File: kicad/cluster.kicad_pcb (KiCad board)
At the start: 2 copper layers, 24.5 x 33.5 mm, 16 parts, among them J1 Conn_01x07

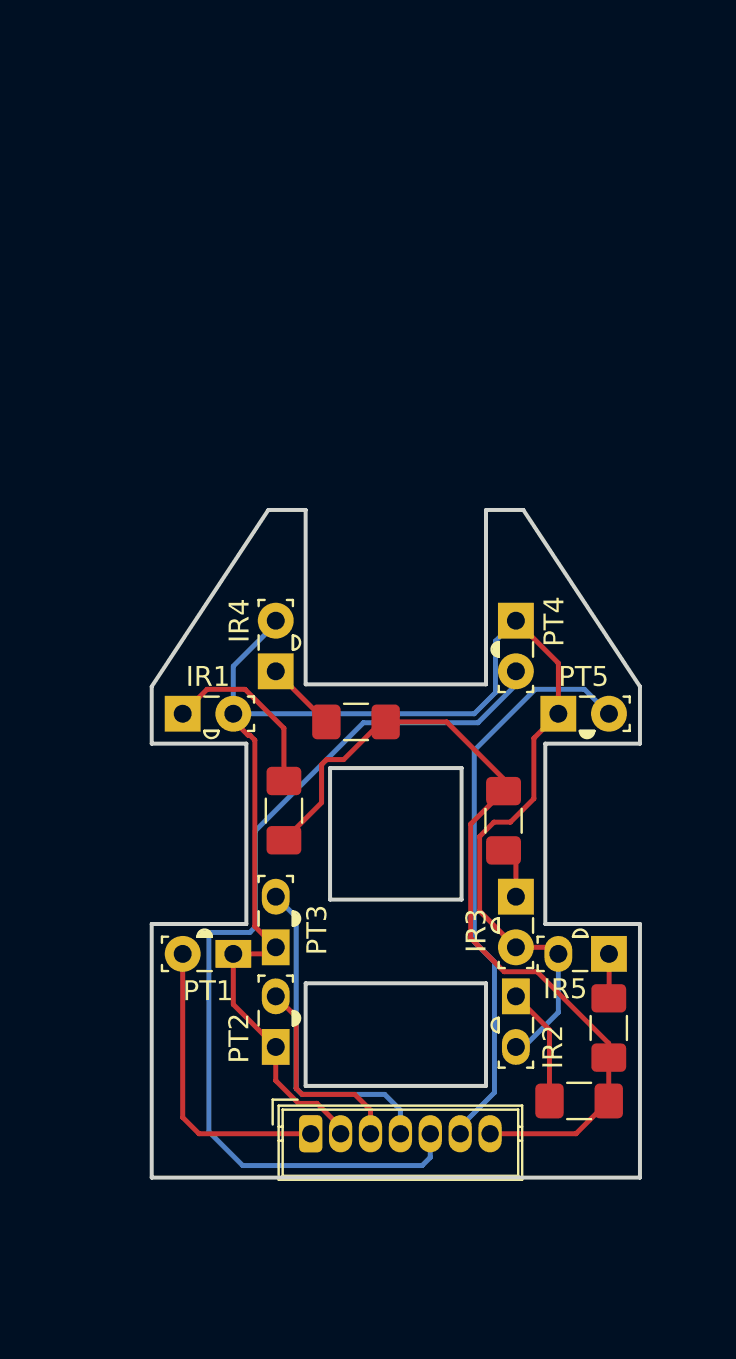
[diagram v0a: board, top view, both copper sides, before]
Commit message: Update the kicad design for the finger cluster
This brings the PCB design up to par with the current cluster design.
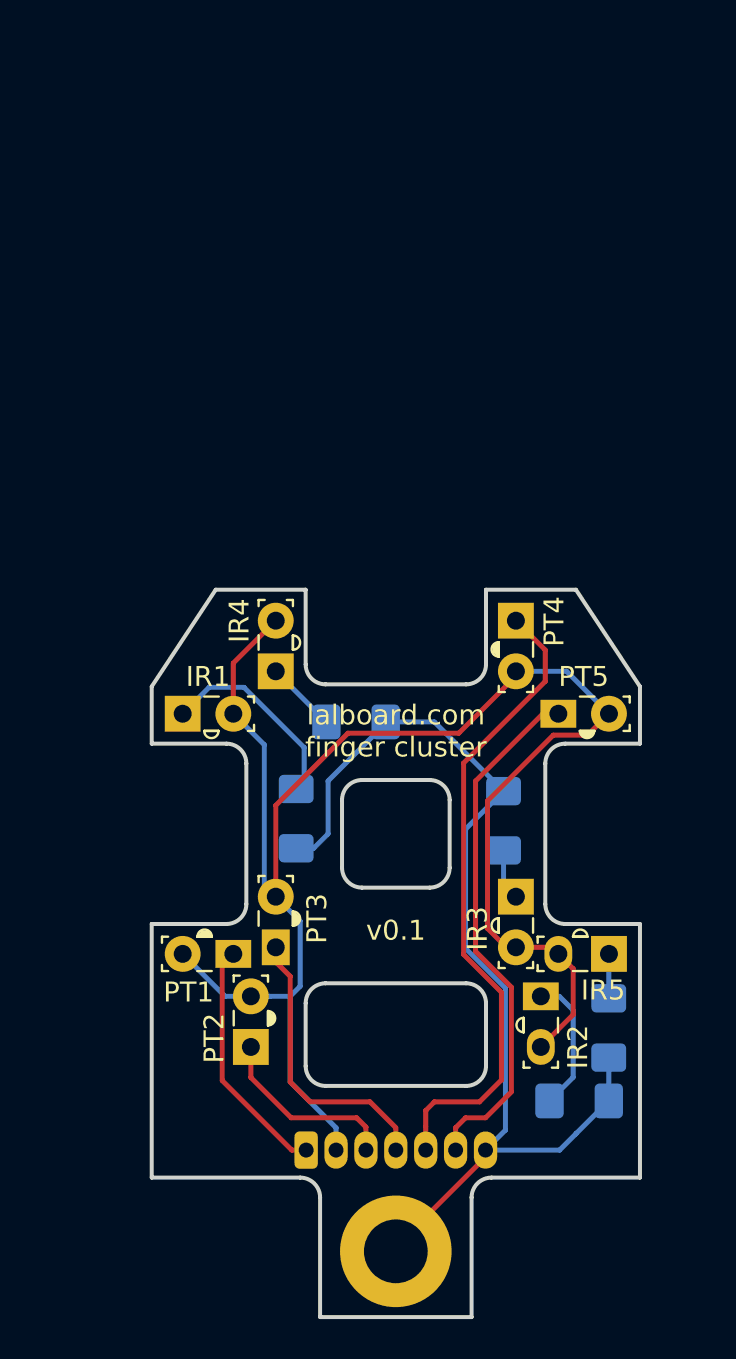
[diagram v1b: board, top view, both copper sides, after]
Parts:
- added REF**: MountingHole_3.2mm_M3, MountingHole:MountingHole_3.2mm_M3_DIN965_Pad, F.Cu at (165.3, 122.0)
- J1: footprint lalboard:JST_ZH_B7B-ZR_1x07_P1.50mm_Vertical -> lalboard:JST_ZH_S7B-ZR_1x07_P1.50mm_Horizontal; moved to B.Cu
- R1, R2, R3, R4, R5: moved to B.Cu
- moved IR2 1.25 mm to (172.6, 109.2)
- moved PT2 1.25 mm to (158.0, 111.8)
- moved J1 0.83 mm to (160.8, 116.9)
- moved R1 0.73 mm to (160.3, 100.3)
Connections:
- PT1 pad 1: +5V -> C1
- PT1 pad 2: C1 -> +5V
- PT2 pad 1: +5V -> C3
- PT2 pad 2: C3 -> +5V
- PT3 pad 1: +5V -> C4
- PT3 pad 2: C4 -> +5V
- PT4 pad 1: +5V -> C5
- PT4 pad 2: C5 -> +5V
- PT5 pad 1: +5V -> C6
- PT5 pad 2: C6 -> +5V
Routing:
- net C5: track 47.2 -> 32.6 mm
- net GND: track 43.5 -> 52.5 mm
- net +5V: track 78.1 -> 86.4 mm
- net C1: track 14.8 -> 12.2 mm
- net C4: track 16.9 -> 14.4 mm
- net C6: track 28.9 -> 26.6 mm
- net Net-(IR2-Pad1): track 5.95 -> 6.96 mm
- net Net-(IR1-Pad1): track 9.04 -> 9.97 mm
- net C3: track 10.4 -> 9.49 mm
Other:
- board size 24.5 x 33.5 mm -> 24.5 x 36.5 mm
- board text added: "Min internal corner radius: .8mm (for all internal corners)"
- board text added: "lalboard.com finger cluster"
- board text added: "v0.1"

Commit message: Update kicad design for finger cluster
This adds ground/+5v planes, some thicker traces, and moves the +5v pin
to pin 1 of the connector.

Thanks to @rutgervana for taking a look at the design and making
suggestions/showing example improvements.
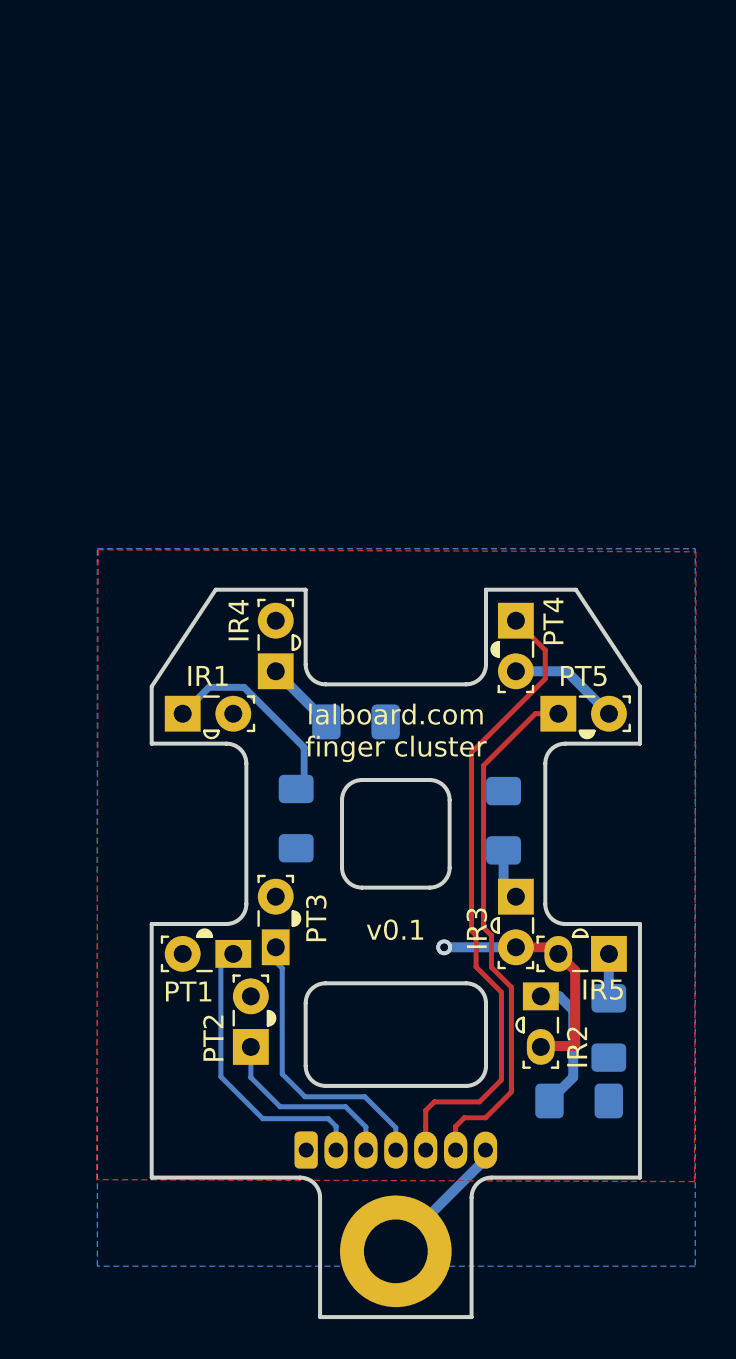
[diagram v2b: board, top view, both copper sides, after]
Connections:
- J1 pad 1: C1 -> +5V
- J1 pad 2: +5V -> C1
- J1 pad 3: C3 -> C2
- J1 pad 4: C4 -> C3
- J1 pad 5: C5 -> C4
- J1 pad 6: C6 -> C5
- PT2 pad 1: C3 -> C2
- PT3 pad 1: C4 -> C3
- PT4 pad 1: C5 -> C4
- PT5 pad 1: C6 -> C5
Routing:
- net +5V: track 86.4 -> 18.4 mm, vias 0 -> 1
- net GND: track 52.5 -> 7.04 mm
- net C6: track 26.6 -> 0.00 mm
- net C4: track 14.4 -> 32.2 mm
- net C2: track 0.00 -> 9.49 mm
- net C5: track 32.6 -> 26.5 mm
- net C3: track 9.49 -> 14.4 mm
- net C1: track 12.2 -> 15.2 mm
- added copper zone on F.Cu, net +5V
- added copper zone on B.Cu, net GND
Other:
- net class Power added: clearance 0.2, trace_width 0.5, via_dia 0.8, via_drill 0.4

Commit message: Add a virtual "locating pin" to the cluster pcb sketch
This gives a reference point for the origin of the sketch, so the import
location can be set correctly when importing the outline into kicad.

Basically, you set the grid origin in kicad to the center of the circle
(assuming the locating pin is already in kicad) and then make a note of
the coordinates of that point. And then, when importing the outline, you
can specify those coordinates as the location, to ensure the origin of the
imported outline matches that of the existing/previous outline.
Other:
- board text added: "Coords for import: (152.85, 125.535)"

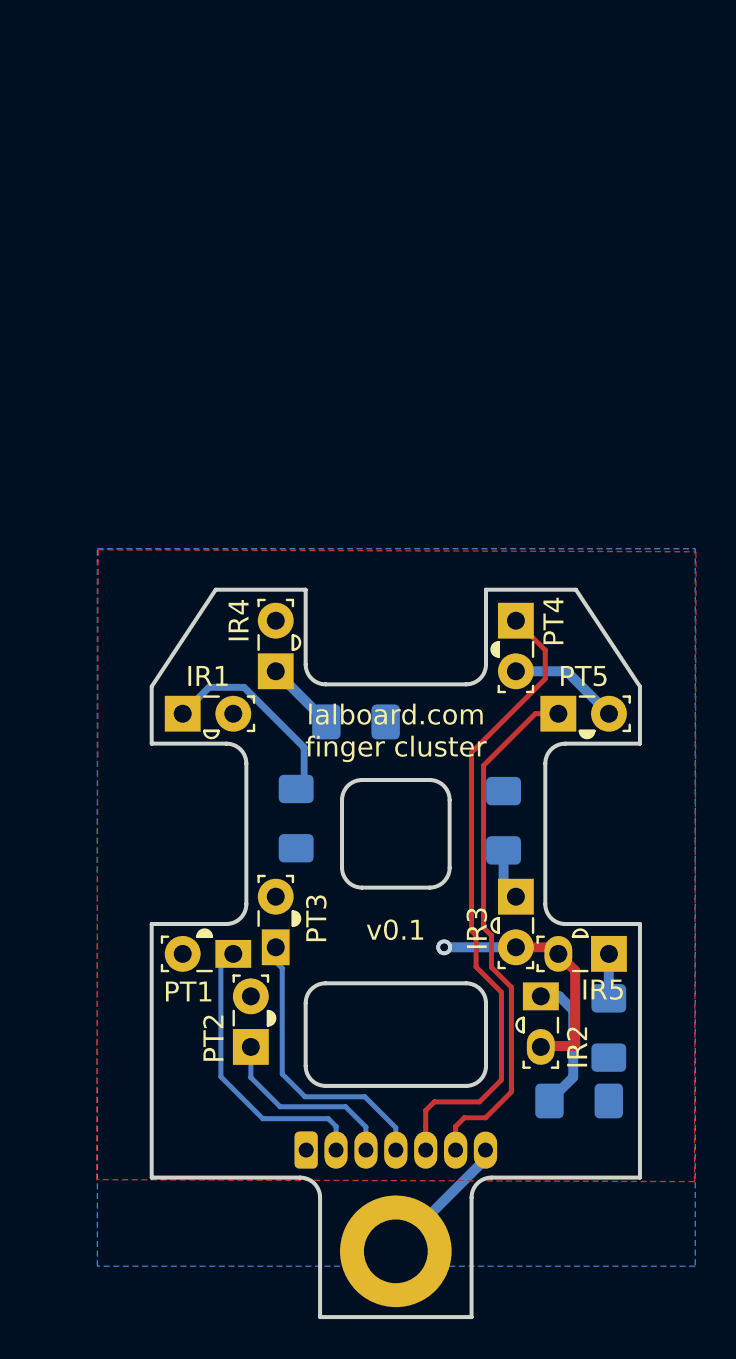
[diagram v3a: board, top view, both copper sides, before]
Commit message: Minor tweaks to the cluster pcb
- Move the identifying text to the bottom layer
- Disable some unused layers
- Move the design so that the import position is at an even (150, 100)
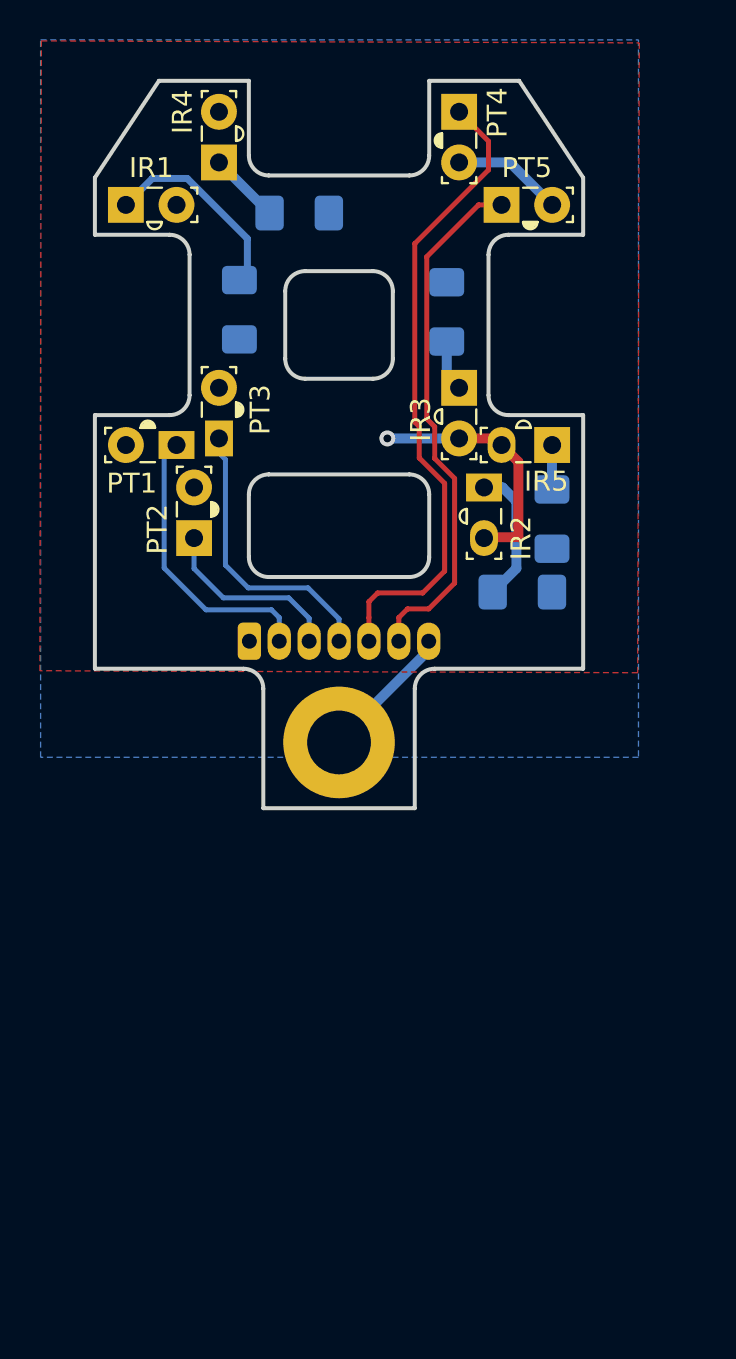
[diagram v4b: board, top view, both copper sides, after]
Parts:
- moved IR4 25.7 mm to (156.4, 67.4)
- moved R1 25.7 mm to (157.4, 74.8)
- moved R3 25.7 mm to (167.9, 74.9)
- moved IR1 25.7 mm to (151.8, 69.5)
- moved IR2 25.7 mm to (169.7, 83.7)
- moved IR3 25.7 mm to (168.5, 78.7)
- moved IR5 25.7 mm to (173.1, 81.6)
- moved J1 25.7 mm to (157.9, 91.4)
- moved PT1 25.7 mm to (154.3, 81.6)
- moved PT2 25.7 mm to (155.2, 86.2)
- moved PT3 25.7 mm to (156.4, 81.2)
- moved PT4 25.7 mm to (168.5, 64.9)
- moved PT5 25.7 mm to (170.6, 69.5)
- moved R2 25.7 mm to (171.6, 89.0)
- moved R4 25.7 mm to (160.5, 69.9)
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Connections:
- IR1 pad 1: Net-(IR1-Pad1) -> (no net)
- IR1 pad 2: +5V -> (no net)
- IR2 pad 1: Net-(IR2-Pad1) -> (no net)
- IR2 pad 2: +5V -> (no net)
- IR3 pad 1: Net-(IR3-Pad1) -> (no net)
- IR3 pad 2: +5V -> (no net)
- IR4 pad 1: Net-(IR4-Pad1) -> (no net)
- IR4 pad 2: +5V -> (no net)
- IR5 pad 1: Net-(IR5-Pad1) -> (no net)
- IR5 pad 2: +5V -> (no net)
- J1 pad 1: +5V -> (no net)
- J1 pad 2: C1 -> (no net)
- J1 pad 3: C2 -> (no net)
- J1 pad 4: C3 -> (no net)
- J1 pad 5: C4 -> (no net)
- J1 pad 6: C5 -> (no net)
- J1 pad 7: GND -> (no net)
- PT1 pad 1: C1 -> (no net)
- PT1 pad 2: +5V -> (no net)
- PT2 pad 1: C2 -> (no net)
- PT2 pad 2: +5V -> (no net)
- PT3 pad 1: C3 -> (no net)
- PT3 pad 2: +5V -> (no net)
- PT4 pad 1: C4 -> (no net)
- PT4 pad 2: +5V -> (no net)
- PT5 pad 1: C5 -> (no net)
- PT5 pad 2: +5V -> (no net)
- R1 pad 1: GND -> (no net)
- R1 pad 2: Net-(IR1-Pad1) -> (no net)
- R2 pad 1: GND -> (no net)
- R2 pad 2: Net-(IR2-Pad1) -> (no net)
- R3 pad 1: GND -> (no net)
- R3 pad 2: Net-(IR3-Pad1) -> (no net)
- R4 pad 1: GND -> (no net)
- R4 pad 2: Net-(IR4-Pad1) -> (no net)
- R5 pad 1: GND -> (no net)
- R5 pad 2: Net-(IR5-Pad1) -> (no net)
- REF** pad 1: GND -> (no net)
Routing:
- net (no net): track 0.00 -> 148.7 mm, vias 0 -> 1
- net C4: track 32.2 -> 0.00 mm
- net C5: track 26.5 -> 0.00 mm
- net +5V: track 18.4 -> 0.00 mm, vias 1 -> 0
- net C1: track 15.2 -> 0.00 mm
- net C3: track 14.4 -> 0.00 mm
- net Net-(IR1-Pad1): track 9.97 -> 0.00 mm
- net C2: track 9.49 -> 0.00 mm
- net GND: track 7.04 -> 0.00 mm
- net Net-(IR2-Pad1): track 6.96 -> 0.00 mm
- net Net-(IR4-Pad1): track 3.59 -> 0.00 mm
- net Net-(IR3-Pad1): track 2.58 -> 0.00 mm
- net Net-(IR5-Pad1): track 2.23 -> 0.00 mm
- added copper zone on B.Cu, net (none)
- added copper zone on F.Cu, net (none)
- removed copper zone on F.Cu, net +5V
- removed copper zone on B.Cu, net GND
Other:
- outline, holes or cut-outs redrawn
- board text added: "Coords for import: (150, 100)"
- board text added: "finger cluster v0.1"
- board text added: "lalboard.com"
- board text removed: "Coords for import: (152.85, 125.535)"
- board text removed: "lalboard.com finger cluster"
- board text removed: "v0.1"

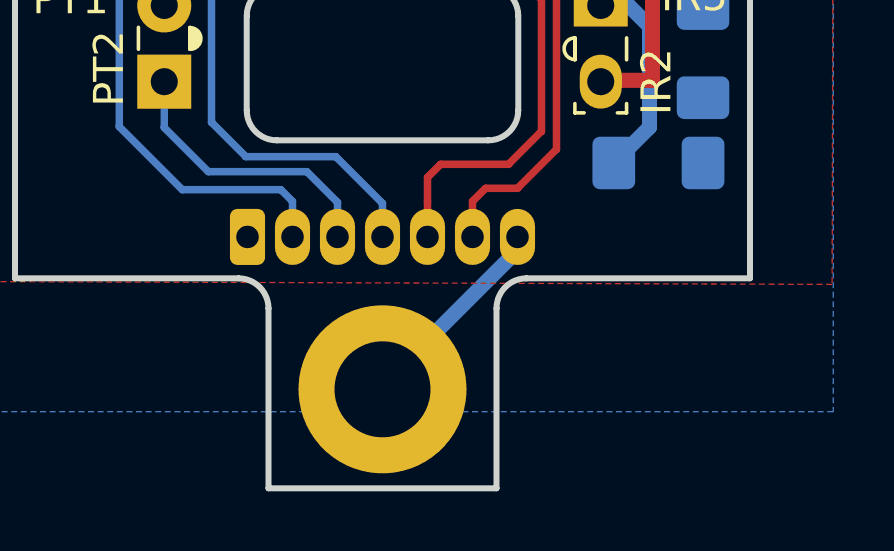
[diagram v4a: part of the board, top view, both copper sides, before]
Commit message: Fix up the cluster and thumb_cluster_left pcbs
Some of the nets for the pours and screw holes had gotten unassigned
somehow
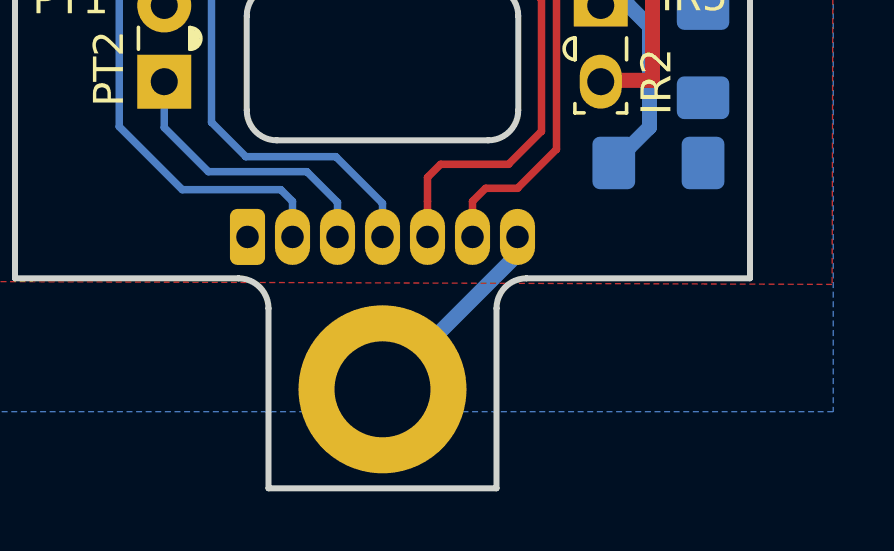
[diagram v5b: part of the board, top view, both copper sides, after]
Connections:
- IR1 pad 1: (no net) -> Net-(IR1-Pad1)
- IR1 pad 2: (no net) -> +5V
- IR2 pad 1: (no net) -> Net-(IR2-Pad1)
- IR2 pad 2: (no net) -> +5V
- IR3 pad 1: (no net) -> Net-(IR3-Pad1)
- IR3 pad 2: (no net) -> +5V
- IR4 pad 1: (no net) -> Net-(IR4-Pad1)
- IR4 pad 2: (no net) -> +5V
- IR5 pad 1: (no net) -> Net-(IR5-Pad1)
- IR5 pad 2: (no net) -> +5V
- J1 pad 1: (no net) -> +5V
- J1 pad 2: (no net) -> C1
- J1 pad 3: (no net) -> C2
- J1 pad 4: (no net) -> C3
- J1 pad 5: (no net) -> C4
- J1 pad 6: (no net) -> C5
- J1 pad 7: (no net) -> GND
- PT1 pad 1: (no net) -> C1
- PT1 pad 2: (no net) -> +5V
- PT2 pad 1: (no net) -> C2
- PT2 pad 2: (no net) -> +5V
- PT3 pad 1: (no net) -> C3
- PT3 pad 2: (no net) -> +5V
- PT4 pad 1: (no net) -> C4
- PT4 pad 2: (no net) -> +5V
- PT5 pad 1: (no net) -> C5
- PT5 pad 2: (no net) -> +5V
- R1 pad 1: (no net) -> GND
- R1 pad 2: (no net) -> Net-(IR1-Pad1)
- R2 pad 1: (no net) -> GND
- R2 pad 2: (no net) -> Net-(IR2-Pad1)
- R3 pad 1: (no net) -> GND
- R3 pad 2: (no net) -> Net-(IR3-Pad1)
- R4 pad 1: (no net) -> GND
- R4 pad 2: (no net) -> Net-(IR4-Pad1)
- R5 pad 1: (no net) -> GND
- R5 pad 2: (no net) -> Net-(IR5-Pad1)
- REF** pad 1: (no net) -> GND
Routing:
- net (no net): track 148.7 -> 0.00 mm, vias 1 -> 0
- net C4: track 0.00 -> 32.2 mm
- net C5: track 0.00 -> 26.5 mm
- net +5V: track 0.00 -> 18.4 mm, vias 0 -> 1
- net C1: track 0.00 -> 15.2 mm
- net C3: track 0.00 -> 14.4 mm
- net Net-(IR1-Pad1): track 0.00 -> 9.97 mm
- net C2: track 0.00 -> 9.49 mm
- net GND: track 0.00 -> 7.76 mm
- net Net-(IR2-Pad1): track 0.00 -> 6.96 mm
- net Net-(IR4-Pad1): track 0.00 -> 3.59 mm
- net Net-(IR3-Pad1): track 0.00 -> 2.58 mm
- net Net-(IR5-Pad1): track 0.00 -> 2.23 mm
- added copper zone on F.Cu, net +5V
- added copper zone on B.Cu, net GND
- removed copper zone on B.Cu, net (none)
- removed copper zone on F.Cu, net (none)
